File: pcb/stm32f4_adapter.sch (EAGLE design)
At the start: 2 parts

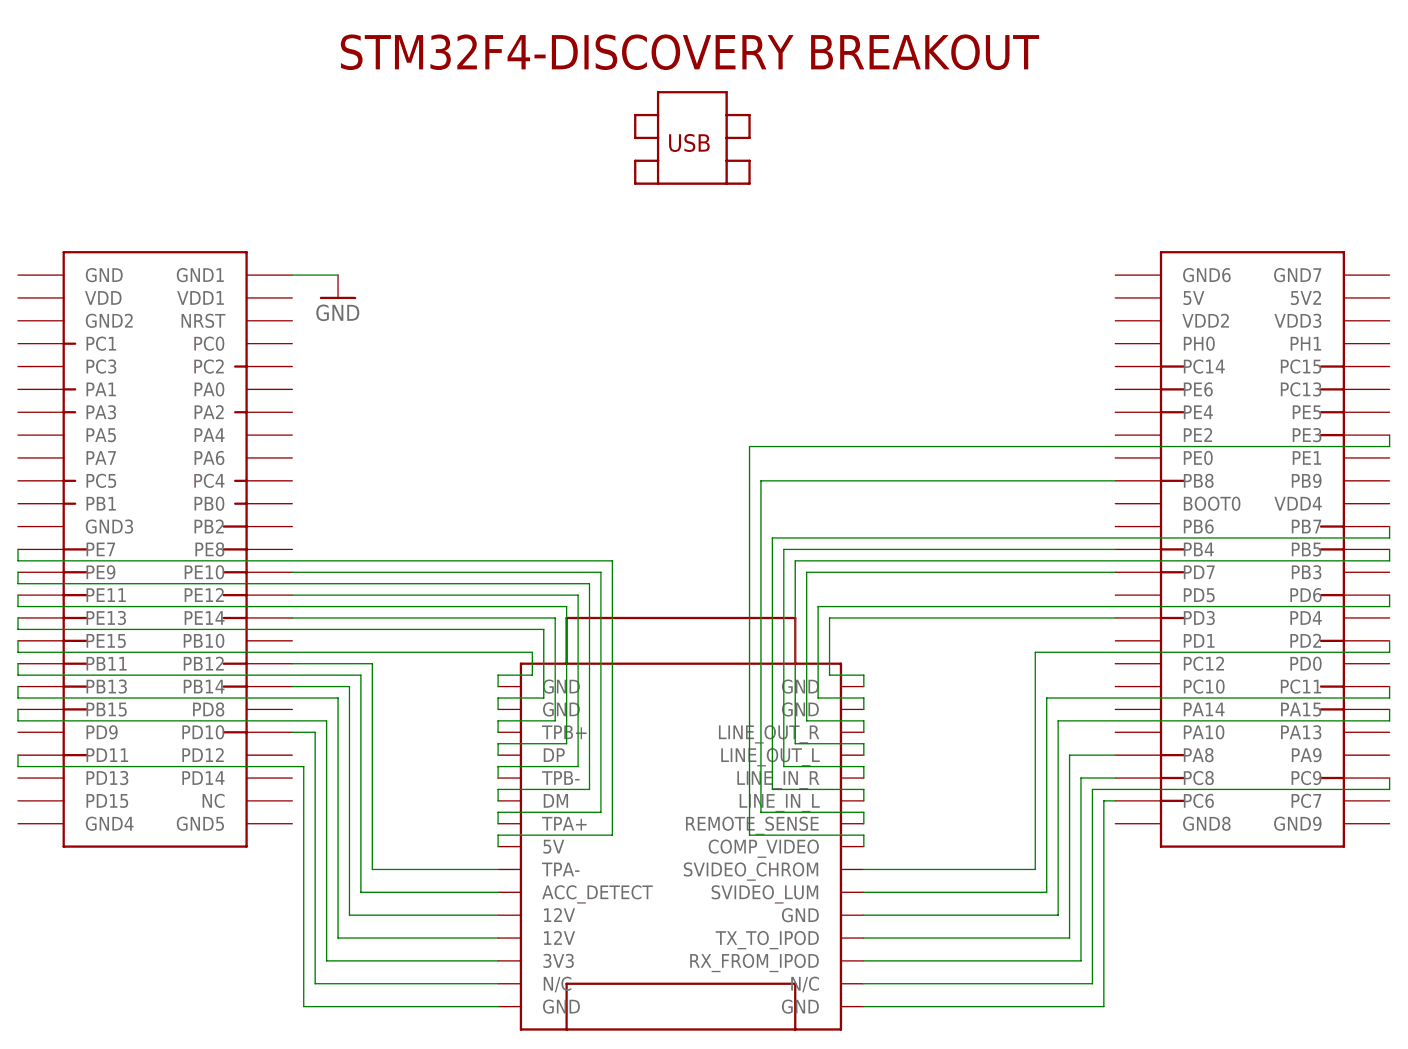
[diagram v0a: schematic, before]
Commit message: Move pin E3 to E2, because E3 is used by CS_I2C/SPI!
For Rev. 2. the STM32F4 Discovery datasheet is lying!
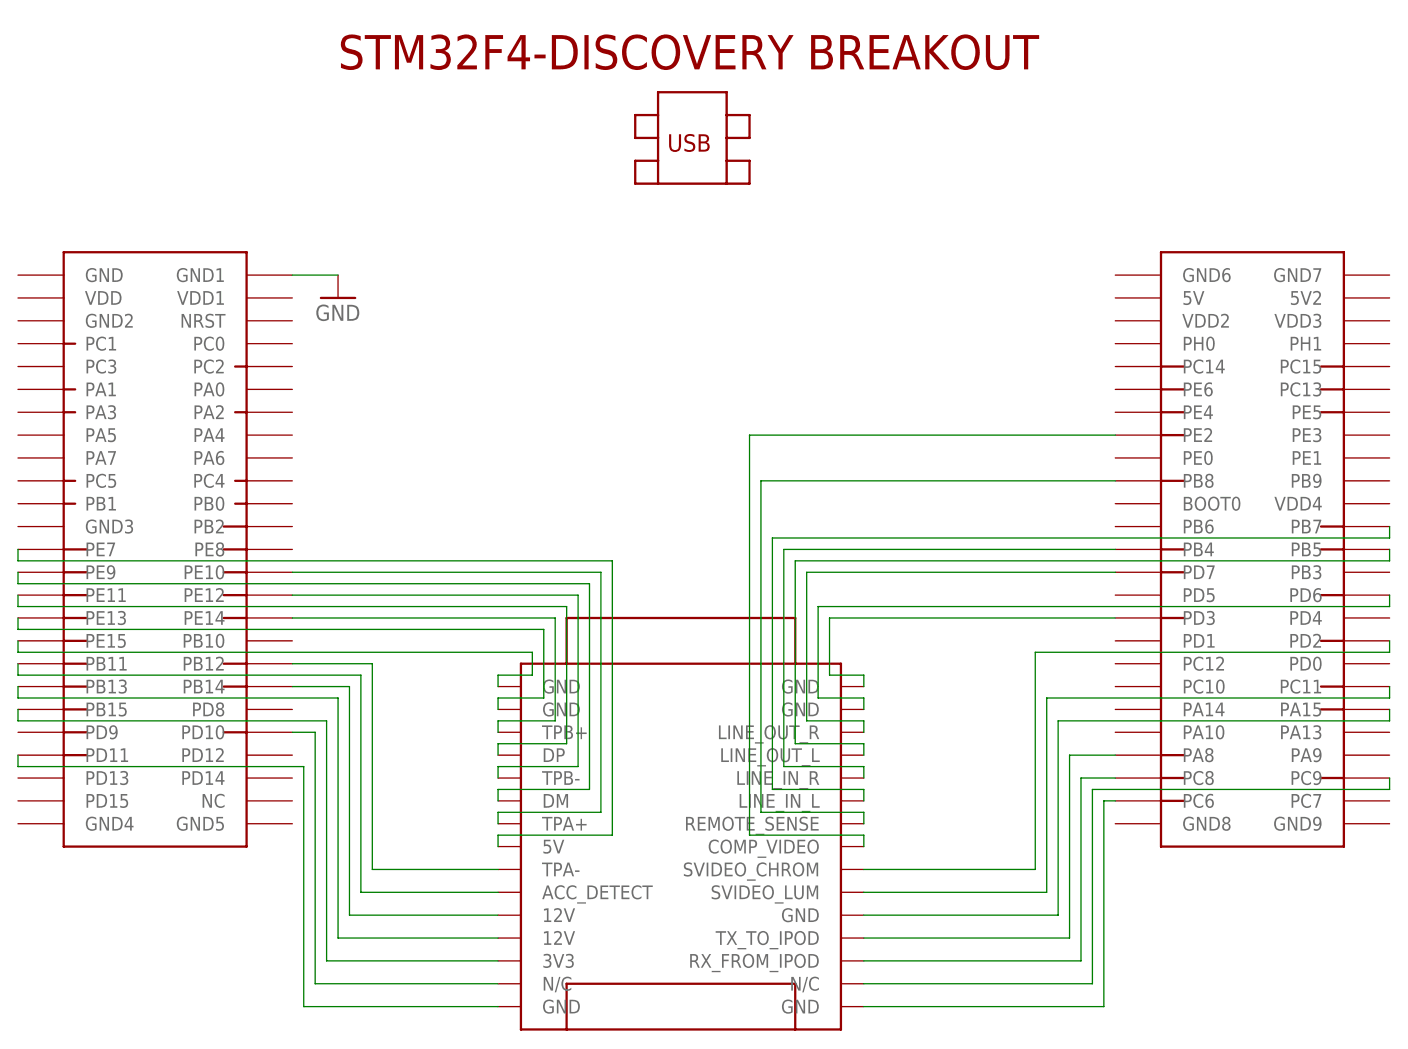
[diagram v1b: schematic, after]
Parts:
- U$1: device STM32F4-DISCOVERY:STM32F4-DISCOVERY -> elva:STM32F4-DISCOVERY
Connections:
- removed net N$30: U$1.PE3, U$2.COMP_VIDEO
- new net N$23: U$1.PE2, U$2.COMP_VIDEO
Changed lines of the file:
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@@
 </classes>
 <parts>
-<part name="U$1" library="STM32F4-DISCOVERY" deviceset="STM32F4-DISCOVERY" device=""/>
+<part name="U$1" library="elva" deviceset="STM32F4-DISCOVERY" device=""/>
 <part name="U$2" library="STM32F4-DISCOVERY" deviceset="IPOD-CONNECTOR" device=""/>
 <part name="GND1" library="supply1" deviceset="GND" device=""/>
@@
 </segment>
 </net>
-<net name="N$30" class="0">
-<segment>
-<pinref part="U$1" gate="G$1" pin="PE3"/>
-<wire x1="7.62" y1="59.69" x2="78.74" y2="59.69" width="0.1524" layer="91"/>
-<wire x1="78.74" y1="59.69" x2="78.74" y2="60.96" width="0.1524" layer="91"/>
-<wire x1="7.62" y1="59.69" x2="7.62" y2="16.51" width="0.1524" layer="91"/>
-<pinref part="U$2" gate="G$1" pin="COMP_VIDEO"/>
-<wire x1="7.62" y1="16.51" x2="20.32" y2="16.51" width="0.1524" layer="91"/>
-<wire x1="20.32" y1="16.51" x2="20.32" y2="15.24" width="0.1524" layer="91"/>
-</segment>
-</net>
 <net name="N$31" class="0">
 <segment>
@@
 </segment>
 </net>
+<net name="N$23" class="0">
+<segment>
+<pinref part="U$1" gate="G$1" pin="PE2"/>
+<wire x1="48.26" y1="60.96" x2="7.62" y2="60.96" width="0.1524" layer="91"/>
+<pinref part="U$2" gate="G$1" pin="COMP_VIDEO"/>
+<wire x1="7.62" y1="60.96" x2="7.62" y2="16.51" width="0.1524" layer="91"/>
+<wire x1="7.62" y1="16.51" x2="20.32" y2="16.51" width="0.1524" layer="91"/>
+<wire x1="20.32" y1="16.51" x2="20.32" y2="15.24" width="0.1524" layer="91"/>
+</segment>
+</net>
